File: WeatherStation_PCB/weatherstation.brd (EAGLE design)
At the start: 59.7 x 53.3 mm, 17 parts

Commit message: Fixed Issue #3 Updated the design to contain the 5V jumper.
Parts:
- added 5V_JUMP: (no value), rcl:R0805
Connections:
- new net N$3: 5V_JUMP.1, U$1.5V
- net 5V: now also 5V_JUMP.2; no longer U$1.5V
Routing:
- net 5V: track 45.4 -> 39.1 mm
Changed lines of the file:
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@@
 <text x="44.45" y="22.86" size="1.778" layer="25" rot="R90">WIND</text>
 <text x="44.45" y="7.62" size="1.778" layer="25" rot="R90">TPH</text>
-<text x="15.24" y="17.78" size="1.778" layer="25" rot="R270">IR &amp; WHITE</text>
-<text x="15.24" y="44.45" size="1.778" layer="25" rot="R270">UV</text>
+<text x="15.24" y="48.26" size="1.778" layer="25" rot="R270">IR &amp; WHITE</text>
+<text x="15.24" y="12.7" size="1.778" layer="25" rot="R270">UV</text>
 <wire x1="37.5" y1="40" x2="22.5" y2="40" width="0.1524" layer="25"/>
 <wire x1="22.5" y1="40" x2="22.5" y2="11" width="0.1524" layer="25"/>
@@
 </element>
 <element name="3P3V_JUMP" library="rcl" package="R0805" value="" x="26.67" y="6.35" smashed="yes" rot="R90">
-<attribute name="NAME" x="27.94" y="6.35" size="0.635" layer="25"/>
+<attribute name="NAME" x="25.4" y="3.81" size="0.635" layer="25" rot="R90"/>
 <attribute name="VALUE" x="29.21" y="5.715" size="1.27" layer="27" rot="R90"/>
 </element>
@@
 <attribute name="NAME" x="3.1115" y="20.7645" size="0.635" layer="25" rot="R90"/>
 </element>
+<element name="5V_JUMP" library="rcl" package="R0805" value="" x="-12.7" y="-3.81"/>
 </elements>
 <signals>
@@
 <contactref element="R3" pad="2"/>
 <contactref element="C3" pad="+"/>
-<contactref element="U$1" pad="5V"/>
 <wire x1="18.05" y1="31.75" x2="18.05" y2="28.26" width="0.635" layer="1"/>
 <wire x1="18.05" y1="28.26" x2="19.37" y2="27.94" width="0.635" layer="1"/>
@@
 <wire x1="19.37" y1="20.32" x2="19.37" y2="18.73" width="0.635" layer="1"/>
 <wire x1="19.37" y1="18.73" x2="26.67" y2="11.43" width="0.635" layer="1"/>
-<wire x1="29.21" y1="2.54" x2="29.21" y2="8.89" width="0.635" layer="1"/>
 <via x="26.67" y="11.43" extent="1-16" drill="0.3302" shape="octagon"/>
 <via x="29.21" y="8.89" extent="1-16" drill="0.3302" shape="octagon"/>
@@
 <via x="17.78" y="27.94" extent="1-16" drill="0.3302" shape="octagon"/>
 <via x="13.7574" y="27.94" extent="1-16" drill="0.3302" shape="octagon"/>
+<contactref element="5V_JUMP" pad="2"/>
+<wire x1="-11.75" y1="-3.81" x2="10.7188" y2="25.1714" width="0" layer="19" extent="1-1"/>
 </signal>
 <signal name="MOSI">
@@
 <wire x1="10.7188" y1="19.6088" x2="10.16" y2="19.05" width="0.635" layer="1"/>
 </signal>
+<signal name="N$3">
+<contactref element="U$1" pad="5V"/>
+<contactref element="5V_JUMP" pad="1"/>
+<wire x1="-13.65" y1="-3.81" x2="29.21" y2="2.54" width="0" layer="19" extent="1-1"/>
+</signal>
 </signals>

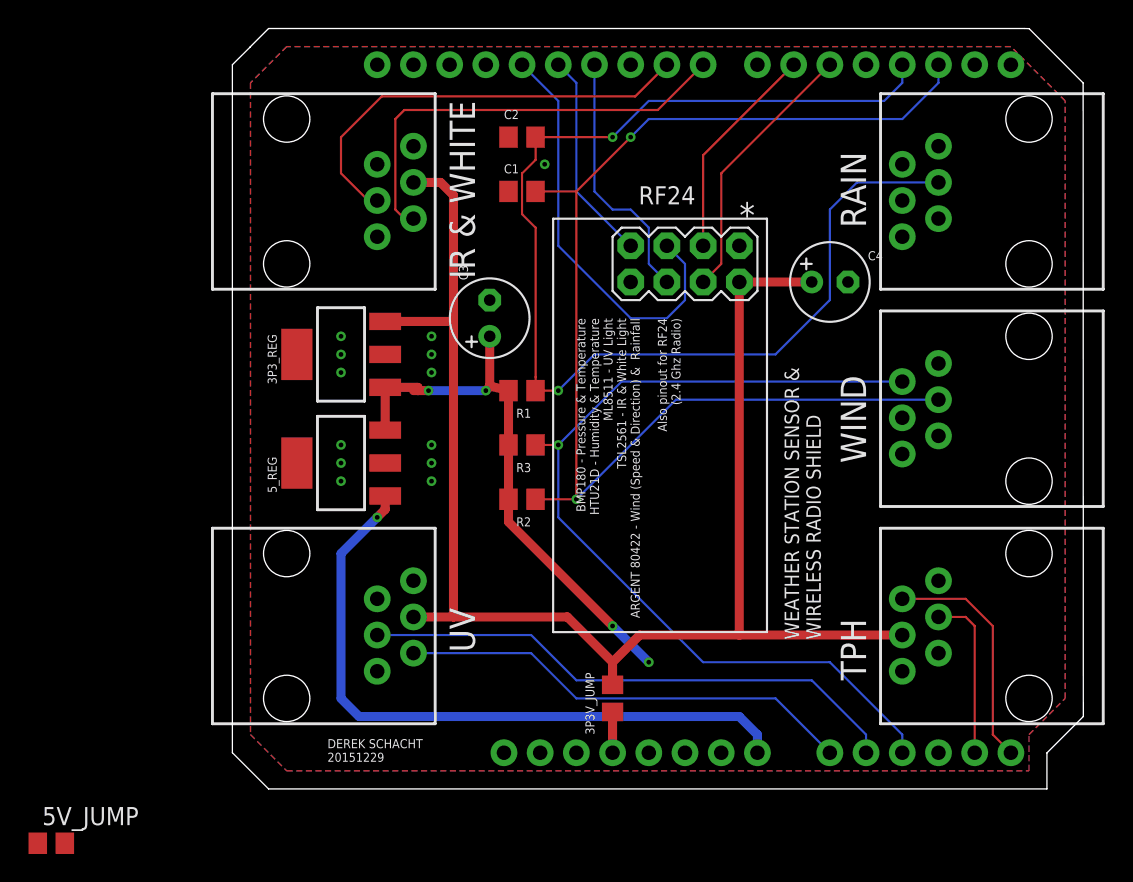
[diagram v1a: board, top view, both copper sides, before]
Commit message: Updated to fix issue #4. The silkscreen now uses 0.03 as the smallest text. Additionally, removed the eagle cache files.
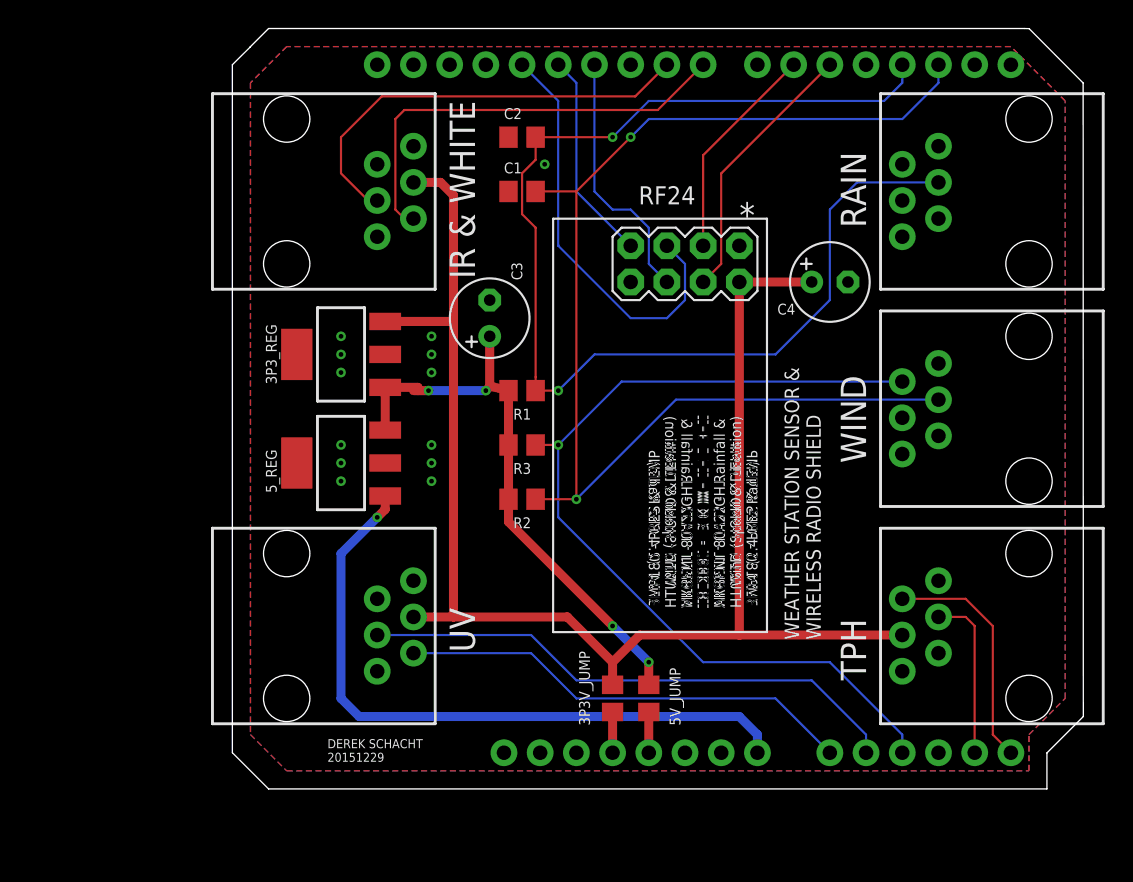
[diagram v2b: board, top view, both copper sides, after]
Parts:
- moved 5V_JUMP 43.1 mm to (29.2, 6.35), turned to 90 degrees
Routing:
- net N$3: track 0.00 -> 2.86 mm
- net 5V: track 39.1 -> 40.7 mm
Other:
- board text added: "BMP180 - PRES & TEMP HTU21D - HUMD & TEMP ML8511 - UV LIGHT TSL2561 - IR & WHITE LIGHT ARGENT 80422 - Rainfall & Wind (Speed & Direction) RF24 (2.4 Ghz Radio)"
- board text removed: "BMP180 - Pressure & Temperature HTU21D - Humidity & Temperature ML8511 - UV Light TSL2561 - IR & White Light ARGENT 80422 - Wind (Speed & Direction) & Rainfall Also pinout for RF24 (2.4 Ghz Radio)"
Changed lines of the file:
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@@
 <text x="41.275" y="10.4775" size="1.016" layer="25" rot="R90">WEATHER STATION SENSOR &amp;
 WIRELESS RADIO SHIELD</text>
-<text x="29.21" y="11.43" size="0.635" layer="26" rot="MR90">BMP180 - Pressure &amp; Temperature
-HTU21D - Humidity &amp; Temperature
-ML8511 - UV Light
-TSL2561 - IR &amp; White Light
-ARGENT 80422 - Wind (Speed &amp; Direction) &amp;  Rainfall
-Also pinout for RF24
-(2.4 Ghz Radio)</text>
-<text x="24.13" y="33.02" size="0.635" layer="25" rot="R270">BMP180 - Pressure &amp; Temperature
-HTU21D - Humidity &amp; Temperature
-ML8511 - UV Light
-TSL2561 - IR &amp; White Light
-ARGENT 80422 - Wind (Speed &amp; Direction) &amp;  Rainfall
-Also pinout for RF24
-(2.4 Ghz Radio)</text>
-<text x="56.515" y="42.2275" size="0.635" layer="26" rot="MR0">RAIN PULSE</text>
-<text x="56.515" y="26.9875" size="0.635" layer="26" rot="MR0">WIND PULSE</text>
-<text x="56.515" y="28.2575" size="0.635" layer="26" rot="MR0">WIND DIR</text>
-<text x="8.5725" y="10.4775" size="0.635" layer="26" rot="MR0">UV_LIGHT</text>
-<text x="8.5725" y="9.2075" size="0.635" layer="26" rot="MR0">UV_ENABLE</text>
-<text x="8.5725" y="11.7475" size="0.635" layer="26" rot="MR0">3P3V</text>
-<text x="8.5725" y="42.2275" size="0.635" layer="26" rot="MR0">3P3V</text>
-<text x="54.61" y="10.4775" size="0.635" layer="26" rot="MR0">3P3V</text>
-<text x="54.61" y="9.2075" size="0.635" layer="26" rot="MR0">GND</text>
-<text x="56.515" y="24.4475" size="0.635" layer="26" rot="MR0">GND</text>
-<text x="56.515" y="25.7175" size="0.635" layer="26" rot="MR0">GND</text>
-<text x="56.515" y="40.9575" size="0.635" layer="26" rot="MR0">GND</text>
-<text x="8.5725" y="43.4975" size="0.635" layer="26" rot="MR0">GND</text>
-<text x="8.5725" y="13.0175" size="0.635" layer="26" rot="MR0">GND</text>
-<text x="54.61" y="13.0175" size="0.635" layer="26" rot="MR0">I2C_CLK</text>
-<text x="8.5725" y="39.6875" size="0.635" layer="26" rot="MR0">I2C_CLK</text>
-<text x="8.5725" y="40.9575" size="0.635" layer="26" rot="MR0">I2C_DTA</text>
-<text x="54.61" y="11.7475" size="0.635" layer="26" rot="MR0">I2C_DTA</text>
+<text x="36.83" y="12.7" size="0.762" layer="25" rot="R90">BMP180 - PRES &amp; TEMP
+HTU21D - HUMD &amp; TEMP
+ML8511 - UV LIGHT
+TSL2561 - IR &amp; WHITE LIGHT
+ARGENT 80422 -   Rainfall &amp;
+     Wind (Speed &amp; Direction)
+RF24  (2.4 Ghz Radio)</text>
+<text x="57.785" y="42.2275" size="0.762" layer="26" rot="MR0">RAIN PULSE</text>
+<text x="57.785" y="26.9875" size="0.762" layer="26" rot="MR0">WIND PULSE</text>
+<text x="57.785" y="28.2575" size="0.762" layer="26" rot="MR0">WIND DIR</text>
+<text x="8.5725" y="10.4775" size="0.762" layer="26" rot="MR0">UV_LIGHT</text>
+<text x="8.5725" y="9.2075" size="0.762" layer="26" rot="MR0">UV_ENABLE</text>
+<text x="8.5725" y="11.7475" size="0.762" layer="26" rot="MR0">3P3V</text>
+<text x="8.5725" y="42.2275" size="0.762" layer="26" rot="MR0">3P3V</text>
+<text x="55.88" y="10.4775" size="0.762" layer="26" rot="MR0">3P3V</text>
+<text x="55.88" y="9.2075" size="0.762" layer="26" rot="MR0">GND</text>
+<text x="57.785" y="24.4475" size="0.762" layer="26" rot="MR0">GND</text>
+<text x="57.785" y="25.7175" size="0.762" layer="26" rot="MR0">GND</text>
+<text x="57.785" y="40.9575" size="0.762" layer="26" rot="MR0">GND</text>
+<text x="8.5725" y="43.4975" size="0.762" layer="26" rot="MR0">GND</text>
+<text x="8.5725" y="13.0175" size="0.762" layer="26" rot="MR0">GND</text>
+<text x="55.88" y="13.0175" size="0.762" layer="26" rot="MR0">I2C_CLK</text>
+<text x="8.5725" y="39.6875" size="0.762" layer="26" rot="MR0">I2C_CLK</text>
+<text x="8.5725" y="40.9575" size="0.762" layer="26" rot="MR0">I2C_DTA</text>
+<text x="55.88" y="11.7475" size="0.762" layer="26" rot="MR0">I2C_DTA</text>
+<text x="29.21" y="12.7" size="0.762" layer="25" rot="MR90">BMP180 - PRES &amp; TEMP
+HTU21D - HUMD &amp; TEMP
+ML8511 - UV LIGHT
+TSL2561 - IR &amp; WHITE LIGHT
+ARGENT 80422 -   Rainfall &amp;
+     Wind (Speed &amp; Direction)
+RF24  (2.4 Ghz Radio)</text>
 </plain>
 <attributes>
@@
 <elements>
 <element name="C1" library="rcl" package="C0805" value="" x="20.32" y="41.91" smashed="yes">
-<attribute name="NAME" x="19.05" y="43.18" size="0.635" layer="25"/>
+<attribute name="NAME" x="19.05" y="43.18" size="0.762" layer="25"/>
 <attribute name="VALUE" x="19.05" y="39.37" size="1.27" layer="27"/>
 </element>
 <element name="C2" library="rcl" package="C0805" value="" x="20.32" y="45.72" smashed="yes">
-<attribute name="NAME" x="19.05" y="46.99" size="0.635" layer="25"/>
+<attribute name="NAME" x="19.05" y="46.99" size="0.762" layer="25"/>
 <attribute name="VALUE" x="19.05" y="43.18" size="1.27" layer="27"/>
 </element>
 <element name="C3" library="rcl" package="E2,5-6" value="" x="18.05" y="33.02" smashed="yes" rot="R90">
-<attribute name="NAME" x="16.526" y="35.687" size="0.635" layer="25" ratio="10" rot="R90"/>
+<attribute name="NAME" x="20.336" y="35.687" size="0.762" layer="25" ratio="10" rot="R90"/>
 <attribute name="VALUE" x="20.717" y="35.687" size="1.27" layer="27" ratio="10" rot="R90"/>
 </element>
 <element name="R1" library="rcl" package="R0805" value="" x="20.32" y="27.94" smashed="yes" rot="R180">
-<attribute name="NAME" x="20.955" y="26.67" size="0.635" layer="25" rot="R180"/>
+<attribute name="NAME" x="20.955" y="26.67" size="0.762" layer="25" rot="R180"/>
 <attribute name="VALUE" x="20.955" y="30.48" size="1.27" layer="27" rot="R180"/>
 </element>
 <element name="R2" library="rcl" package="R0805" value="" x="20.32" y="20.32" smashed="yes" rot="R180">
-<attribute name="NAME" x="20.955" y="19.05" size="0.635" layer="25" rot="R180"/>
+<attribute name="NAME" x="20.955" y="19.05" size="0.762" layer="25" rot="R180"/>
 <attribute name="VALUE" x="20.955" y="22.86" size="1.27" layer="27" rot="R180"/>
 </element>
 <element name="R3" library="rcl" package="R0805" value="" x="20.32" y="24.13" smashed="yes" rot="R180">
-<attribute name="NAME" x="20.955" y="22.86" size="0.635" layer="25" rot="R180"/>
+<attribute name="NAME" x="20.955" y="22.86" size="0.762" layer="25" rot="R180"/>
 <attribute name="VALUE" x="20.955" y="26.67" size="1.27" layer="27" rot="R180"/>
 </element>
@@
 <element name="LIGHT2" library="SparkFun-Connectors" package="RJ11-6" value="RJ11-6PTH" x="3.81" y="16.51" rot="R270"/>
 <element name="C4" library="rcl" package="E2,5-6" value="" x="41.91" y="35.56" smashed="yes">
-<attribute name="NAME" x="44.577" y="37.084" size="0.635" layer="25" ratio="10"/>
+<attribute name="NAME" x="38.227" y="33.274" size="0.762" layer="25" ratio="10"/>
 <attribute name="VALUE" x="44.577" y="32.893" size="1.27" layer="27" ratio="10"/>
 </element>
 <element name="3P3_REG" library="SparkFun-PowerIC" package="SOT223" value="V_REG_MIC2920" x="7.62" y="30.48" smashed="yes" rot="R90">
-<attribute name="NAME" x="3.1115" y="28.3845" size="0.635" layer="25" rot="R90"/>
+<attribute name="NAME" x="3.1115" y="28.3845" size="0.762" layer="25" rot="R90"/>
 </element>
 <element name="3P3V_JUMP" library="rcl" package="R0805" value="" x="26.67" y="6.35" smashed="yes" rot="R90">
-<attribute name="NAME" x="25.4" y="3.81" size="0.635" layer="25" rot="R90"/>
+<attribute name="NAME" x="25.0825" y="4.445" size="0.762" layer="25" rot="R90"/>
 <attribute name="VALUE" x="29.21" y="5.715" size="1.27" layer="27" rot="R90"/>
 </element>
 <element name="5_REG" library="SparkFun-PowerIC" package="SOT223" value="V_REG_MIC2920" x="7.62" y="22.86" smashed="yes" rot="R90">
-<attribute name="NAME" x="3.1115" y="20.7645" size="0.635" layer="25" rot="R90"/>
-</element>
-<element name="5V_JUMP" library="rcl" package="R0805" value="" x="-12.7" y="-3.81"/>
+<attribute name="NAME" x="3.1115" y="20.7645" size="0.762" layer="25" rot="R90"/>
+</element>
+<element name="5V_JUMP" library="rcl" package="R0805" value="" x="29.21" y="6.35" smashed="yes" rot="R90">
+<attribute name="NAME" x="31.4325" y="4.445" size="0.762" layer="25" rot="R90"/>
+<attribute name="VALUE" x="31.75" y="5.715" size="1.27" layer="27" rot="R90"/>
+</element>
 </elements>
 <signals>
@@
 <via x="13.7574" y="27.94" extent="1-16" drill="0.3302" shape="octagon"/>
 <contactref element="5V_JUMP" pad="2"/>
-<wire x1="-11.75" y1="-3.81" x2="10.7188" y2="25.1714" width="0" layer="19" extent="1-1"/>
+<wire x1="29.21" y1="8.89" x2="29.21" y2="7.3" width="0.635" layer="1"/>
 </signal>
 <signal name="MOSI">
@@
 <contactref element="U$1" pad="5V"/>
 <contactref element="5V_JUMP" pad="1"/>
-<wire x1="-13.65" y1="-3.81" x2="29.21" y2="2.54" width="0" layer="19" extent="1-1"/>
+<wire x1="29.21" y1="2.54" x2="29.21" y2="5.4" width="0.635" layer="1"/>
 </signal>
 </signals>
